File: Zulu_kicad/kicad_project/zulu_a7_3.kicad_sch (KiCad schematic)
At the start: 24 parts, among them U3 AS4C32M16SB-7TCN, U4 W25Q128JVSIQ, X3 DM3D-SF

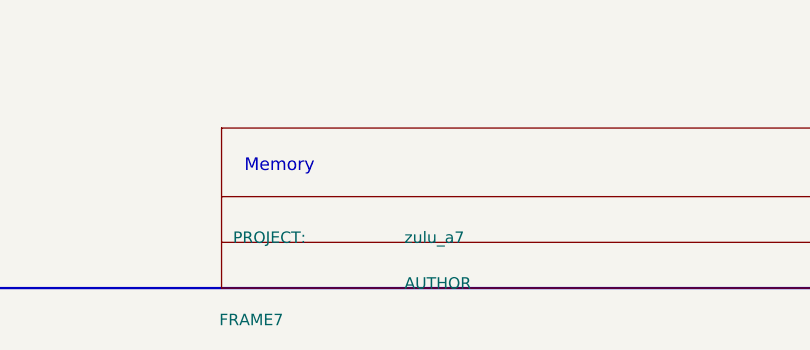
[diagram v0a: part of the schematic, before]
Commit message: Show "AUTHOR: Christian Tambe" in every schematic title block
The EAGLE title block reads "AUTHOR: >AUTHOR" (>AUTHOR = Christian Tambe).
The Altium EAGLE importer left the DOCFIELD AUTHOR parameter as the
literal word "AUTHOR" and dropped the "AUTHOR:" label, and the KiCad
conversion inherited the placeholder.

- Altium (production and HDI_Optimized, 7 SchDocs each):
  tools/schematic_author.py sets the AUTHOR parameter to "Christian Tambe"
  and appends an "AUTHOR:" label at the PROJECT: column in its font, then
  updates the header Weight; every other record stays byte-identical.
  Checked in Altium (sheets 1 and 3) and with the ECO preview, which shows
  only the usual never-executed baseline.
- KiCad: tools/apply_schematic_author.py sets the AUTHOR property and adds
  an AUTHOR_LABEL property. PDF plot shows the row on all 7 pages; netlist
  identical, ERC 1,648 unchanged.
- Docs: docs/schematic_author.md, HDI notes, CONVERSION.md, README notices.
  Zulu_Altrium/ and Altium_backup/ are left as historical snapshots.

Co-Authored-By: Claude Opus 5.5 <noreply@anthropic.com>
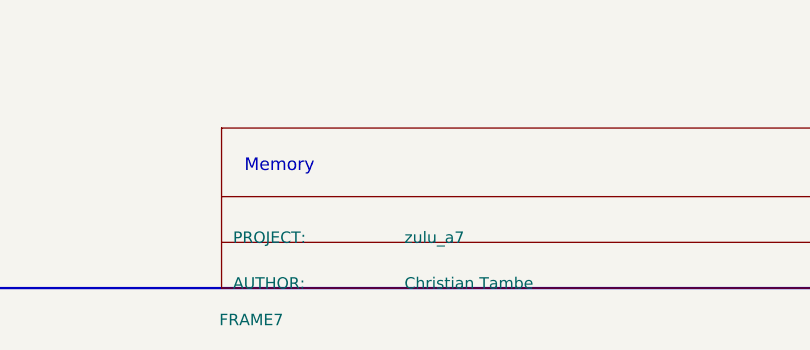
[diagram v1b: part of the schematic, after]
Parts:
- FRAME7: AUTHOR AUTHOR -> Christian Tambe; AUTHOR_LABEL (none) -> AUTHOR:
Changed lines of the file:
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@@
 			)
 		)
-		(property "AUTHOR" "AUTHOR"
+		(property "AUTHOR" "Christian Tambe"
 			(at 116.84 316.484 90)
 			(show_name no)
 			(do_not_autoplace no)
+			(effects
+				(font
+					(size 1.27 1.27)
+				)
+				(justify right bottom)
+			)
+		)
+		(property "AUTHOR_LABEL" "AUTHOR:"
+			(at 97.79 316.484 90)
+			(show_name no)
+			(do_not_autoplace no)
